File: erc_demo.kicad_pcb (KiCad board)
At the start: 2 copper layers, 4 parts, among them J1 Conn_01x01, J2 Conn_01x01

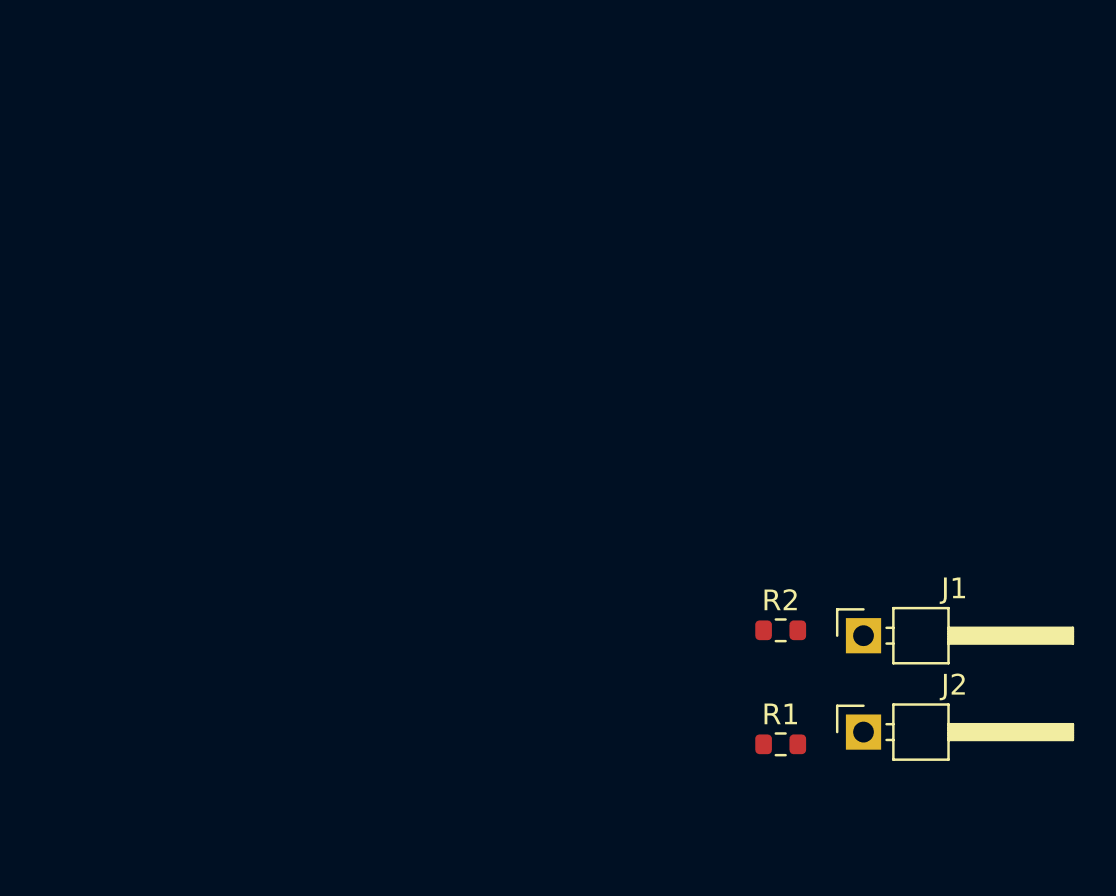
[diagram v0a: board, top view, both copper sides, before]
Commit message: feat: add a hierarchy name demo
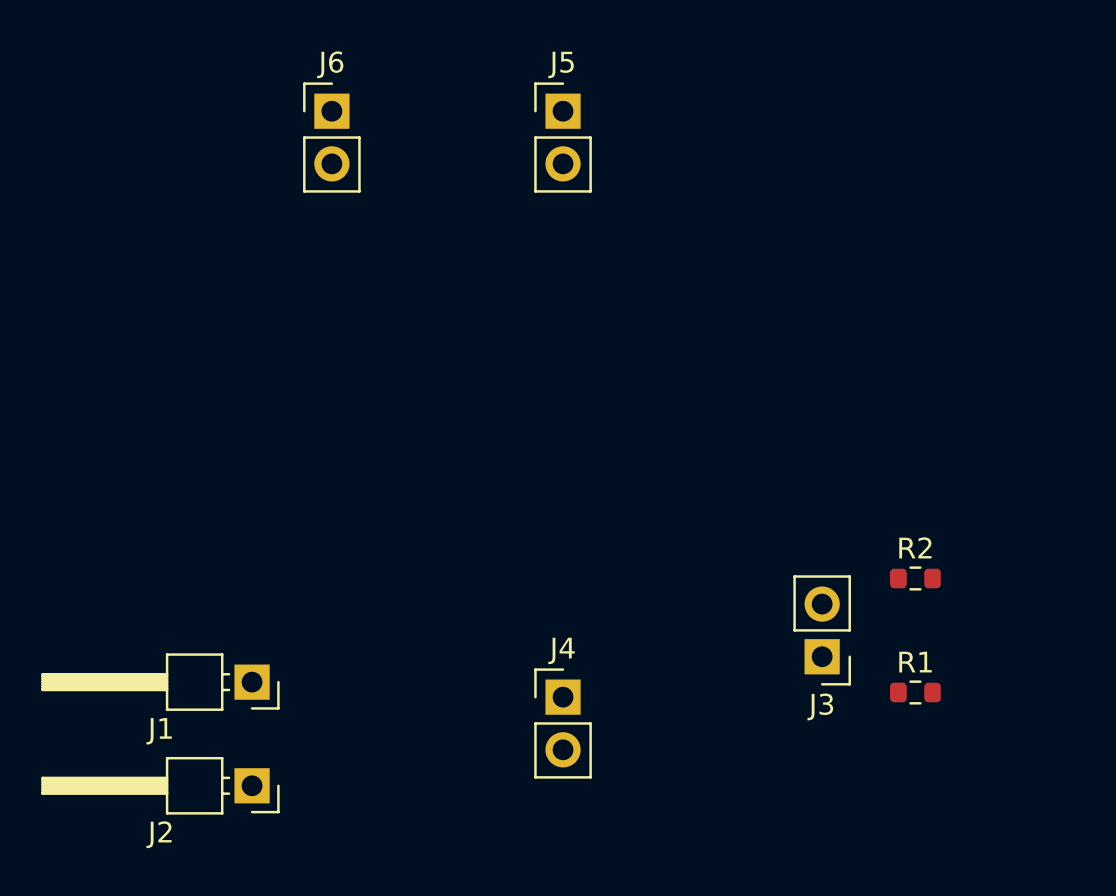
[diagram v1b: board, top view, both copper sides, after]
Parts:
- added J3: Conn_01x02, Connector_PinHeader_2.54mm:PinHeader_1x02_P2.54mm_Vertical, F.Cu at (85.0, 62.8)
- added J4: Conn_01x02, Connector_PinHeader_2.54mm:PinHeader_1x02_P2.54mm_Vertical, F.Cu at (72.5, 64.7)
- added J5: Conn_01x02, Connector_PinHeader_2.54mm:PinHeader_1x02_P2.54mm_Vertical, F.Cu at (72.5, 36.5)
- added J6: Conn_01x02, Connector_PinHeader_2.54mm:PinHeader_1x02_P2.54mm_Vertical, F.Cu at (61.4, 36.5)
- moved J2 29.6 mm to (57.5, 69.0), turned to 180 degrees
- moved J1 29.6 mm to (57.5, 64.0), turned to 180 degrees
- moved R1 6.96 mm to (89.5, 64.5)
- moved R2 6.96 mm to (89.5, 59.0)
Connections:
- J1 pad 1: Net-(J1-Pin_1) -> /USB_M
- J2 pad 1: Net-(J2-Pin_1) -> /USB_P
